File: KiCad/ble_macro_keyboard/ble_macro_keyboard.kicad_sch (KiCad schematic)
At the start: 29 parts, among them SW11 SW_Push, SW12 SW_Push, U1 MCP73831T-2ACI/OT, U2 ESP32-DEVKITC-32D

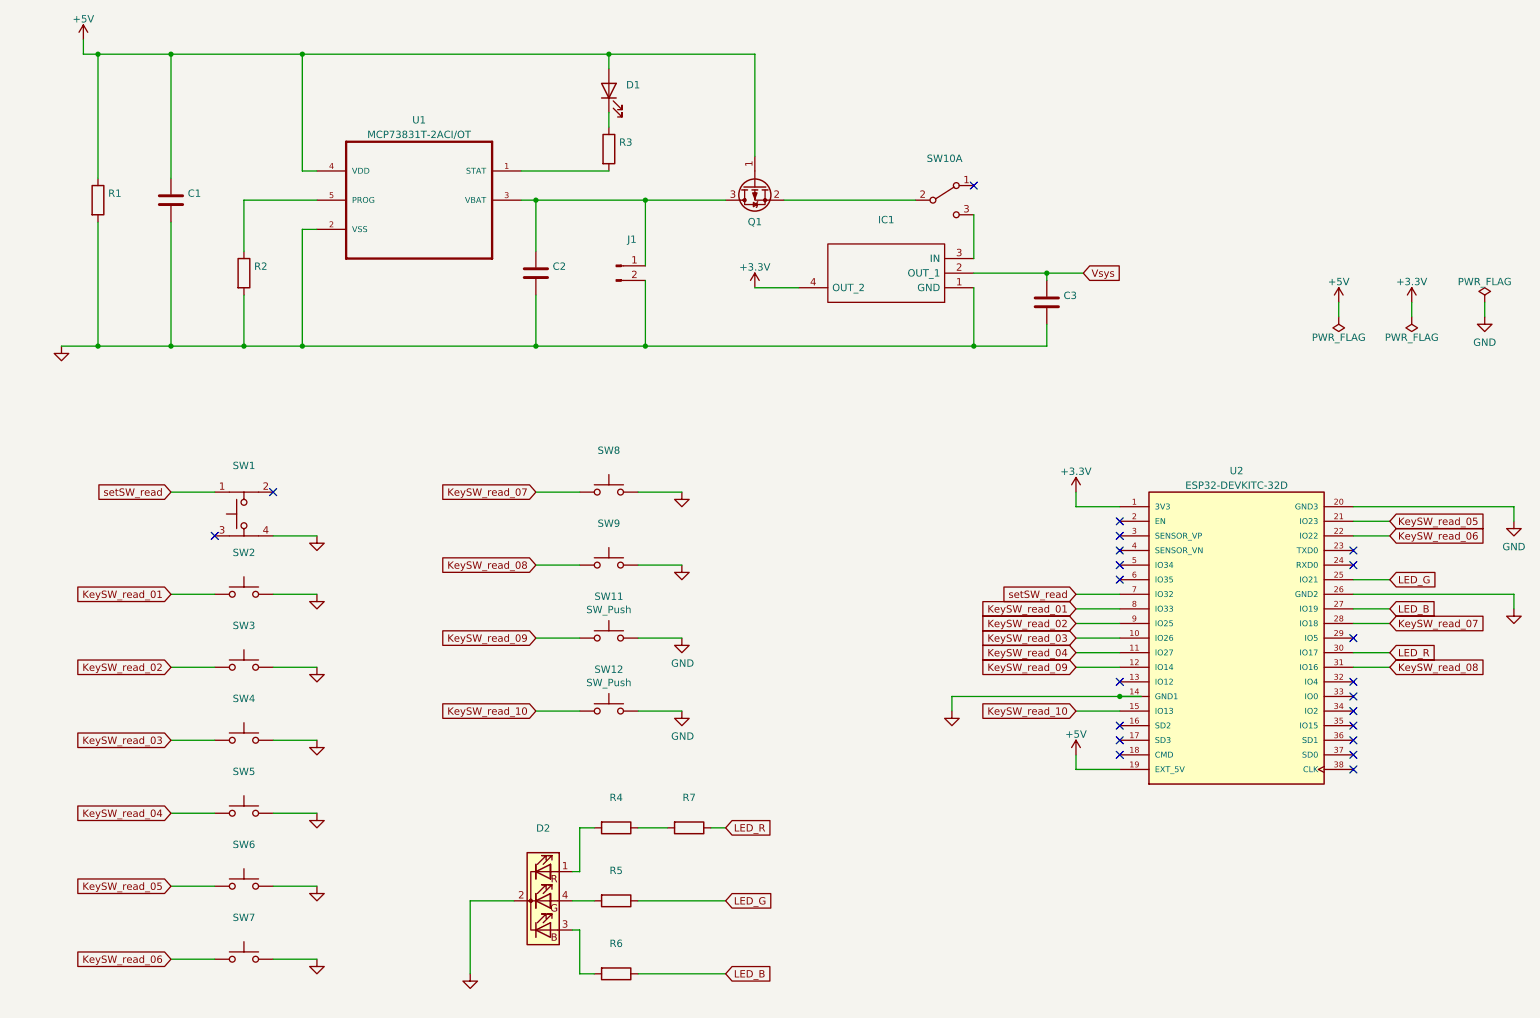
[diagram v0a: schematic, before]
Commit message: library replace and connect symbol to footprint.
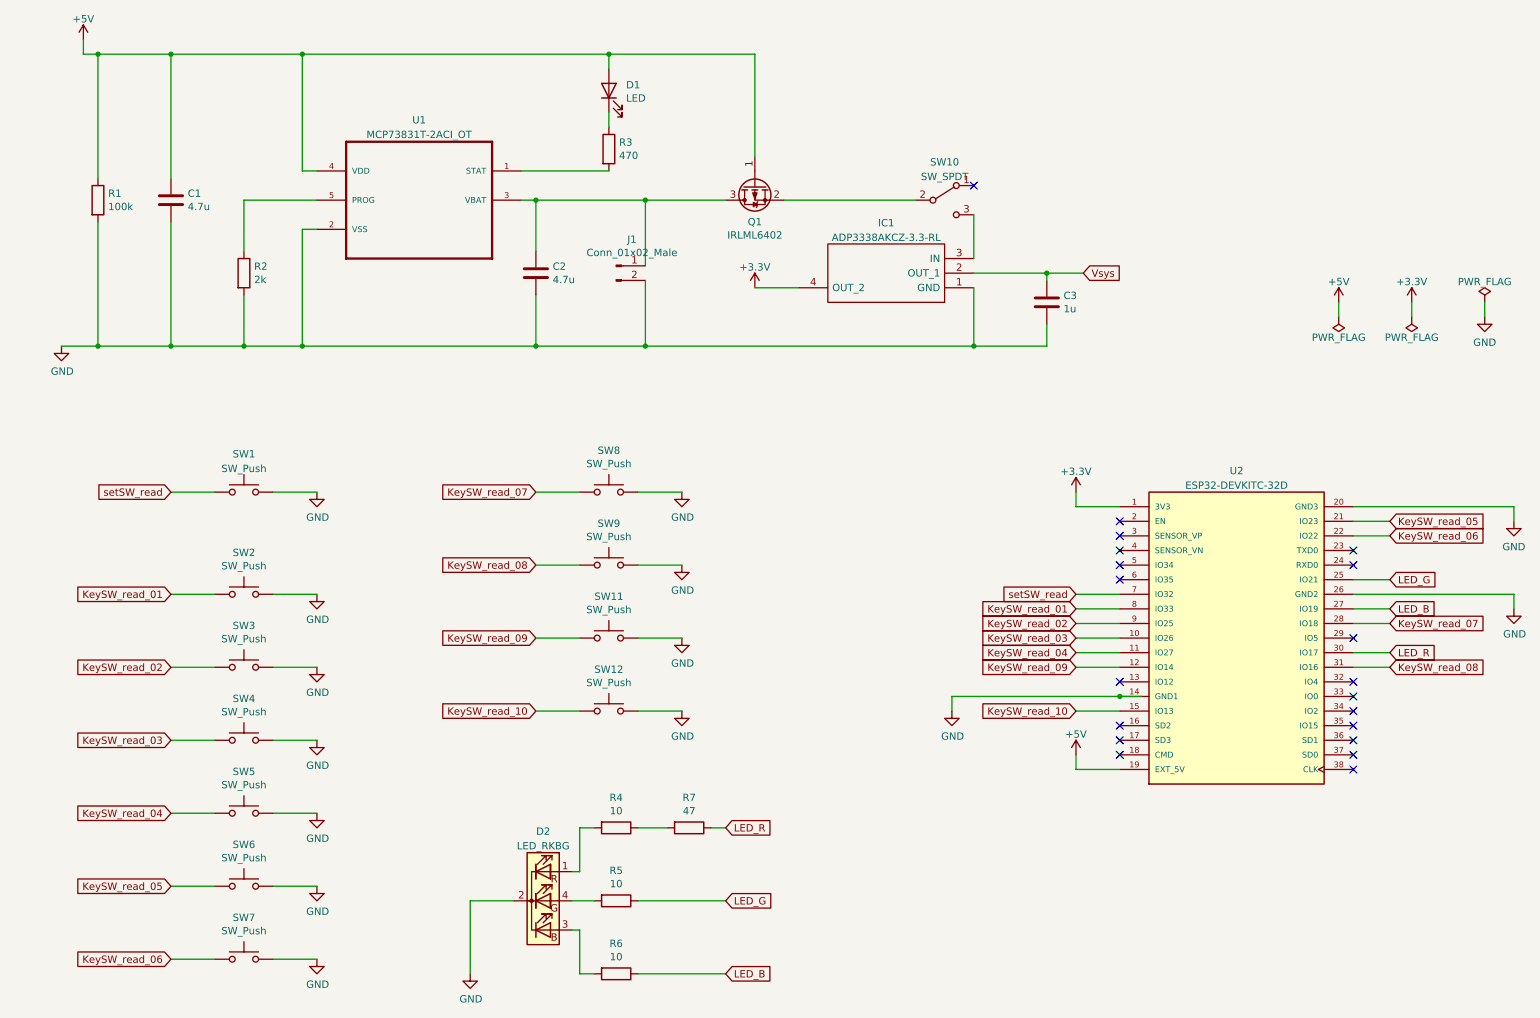
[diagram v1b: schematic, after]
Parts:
- removed D2: (no value), symbol ble_macro_keyboard-rescue:LED_RCBG-Device
- removed IC1: (no value), symbol Regulator_Linear_add:ADP3338AKCZ-3.3-RL
- removed SW1: (no value), symbol Switch_add:SW_SKRPACE010
- removed SW10: (no value), symbol Switch:SW_DPDT_x2
- removed U1: MCP73831T-2ACI/OT, SOT95P280X145-5N, symbol Battery_Management_add:MCP73831T-2ACI/OT
- added D2: LED_RKBG, LED_THT:LED_D5.0mm-4_RGB, symbol Device:LED_RKBG
- added IC1: ADP3338AKCZ-3.3-RL, Ble_keyboard:SOT230P700X180-4N, symbol ble_keyboard:ADP3338AKCZ-3.3-RL
- added SW1: SW_Push, Ble_keyboard:SW_Push_Dual_x2_TS-4401, symbol Switch:SW_Push
- added SW10: SW_SPDT, Ble_keyboard:SW_Slide_SPDT_MSK-12C02, symbol Switch:SW_SPDT
- added U1: MCP73831T-2ACI_OT, Ble_keyboard:SOT95P280X145-5N, symbol ble_keyboard:MCP73831T-2ACI_OT
- C1: value (none) -> 4.7u; footprint (none) -> Capacitor_THT:CP_Radial_D5.0mm_P2.00mm
- C2: value (none) -> 4.7u; footprint (none) -> Capacitor_SMD:C_0805_2012Metric_Pad1.15x1.40mm_HandSolder
- C3: value (none) -> 1u; footprint (none) -> Capacitor_SMD:C_0805_2012Metric_Pad1.15x1.40mm_HandSolder
- D1: value (none) -> LED; footprint (none) -> LED_THT:LED_D3.0mm
- J1: value (none) -> Conn_01x02_Male; footprint (none) -> Connector_JST:JST_SH_SM03B-SRSS-TB_1x03-1MP_P1.00mm_Horizontal
- Q1: value (none) -> IRLML6402; footprint (none) -> Package_TO_SOT_SMD:SOT-23
- R1: value (none) -> 100k; footprint (none) -> Resistor_SMD:R_0603_1608Metric_Pad1.05x0.95mm_HandSolder
- R2: value (none) -> 2k; footprint (none) -> Resistor_SMD:R_0603_1608Metric_Pad1.05x0.95mm_HandSolder
- R3: value (none) -> 470; footprint (none) -> Resistor_SMD:R_0603_1608Metric_Pad1.05x0.95mm_HandSolder
- R4, R5, R6: value (none) -> 10; footprint (none) -> Resistor_SMD:R_0603_1608Metric_Pad1.05x0.95mm_HandSolder
- R7: value (none) -> 47; footprint (none) -> Resistor_SMD:R_0603_1608Metric_Pad1.05x0.95mm_HandSolder
- SW2, SW3, SW4, SW5, SW6, SW7, SW8, SW9: value (none) -> SW_Push; footprint (none) -> Keyswitches:Kailh_socket_MX
- U2: footprint MODULE_ESP32-DEVKITC-32D -> Evaluation_board:MODULE_ESP32-DEVKITC-32D
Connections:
- net +3.3V: now also IC1.4 (OUT_2)
- net +5V: now also U1.4 (VDD)
- net GND: now also D2.2 (K), IC1.1 (GND), SW1.2, U1.2 (VSS)
- net Vsys: now also IC1.2 (OUT_1)
- net setSW_read: now also SW1.1
- net at R2.1: now also U1.5 (PROG)
- net at C2.1, J1.1 (Pin_1), Q1.3 (D): now also U1.3 (VBAT)
- net at Q1.2 (S): now also SW10.2 (B)
- net at R3.2: now also U1.1 (STAT)
- net at R5.2: now also D2.4 (GA)
- net at R4.2: now also D2.1 (RA)
- net at R6.2: now also D2.3 (BA)
- new net: IC1.3 (IN), SW10.3 (C)
- no-connect marks 22 -> 20

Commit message: keyswitch add to 12.
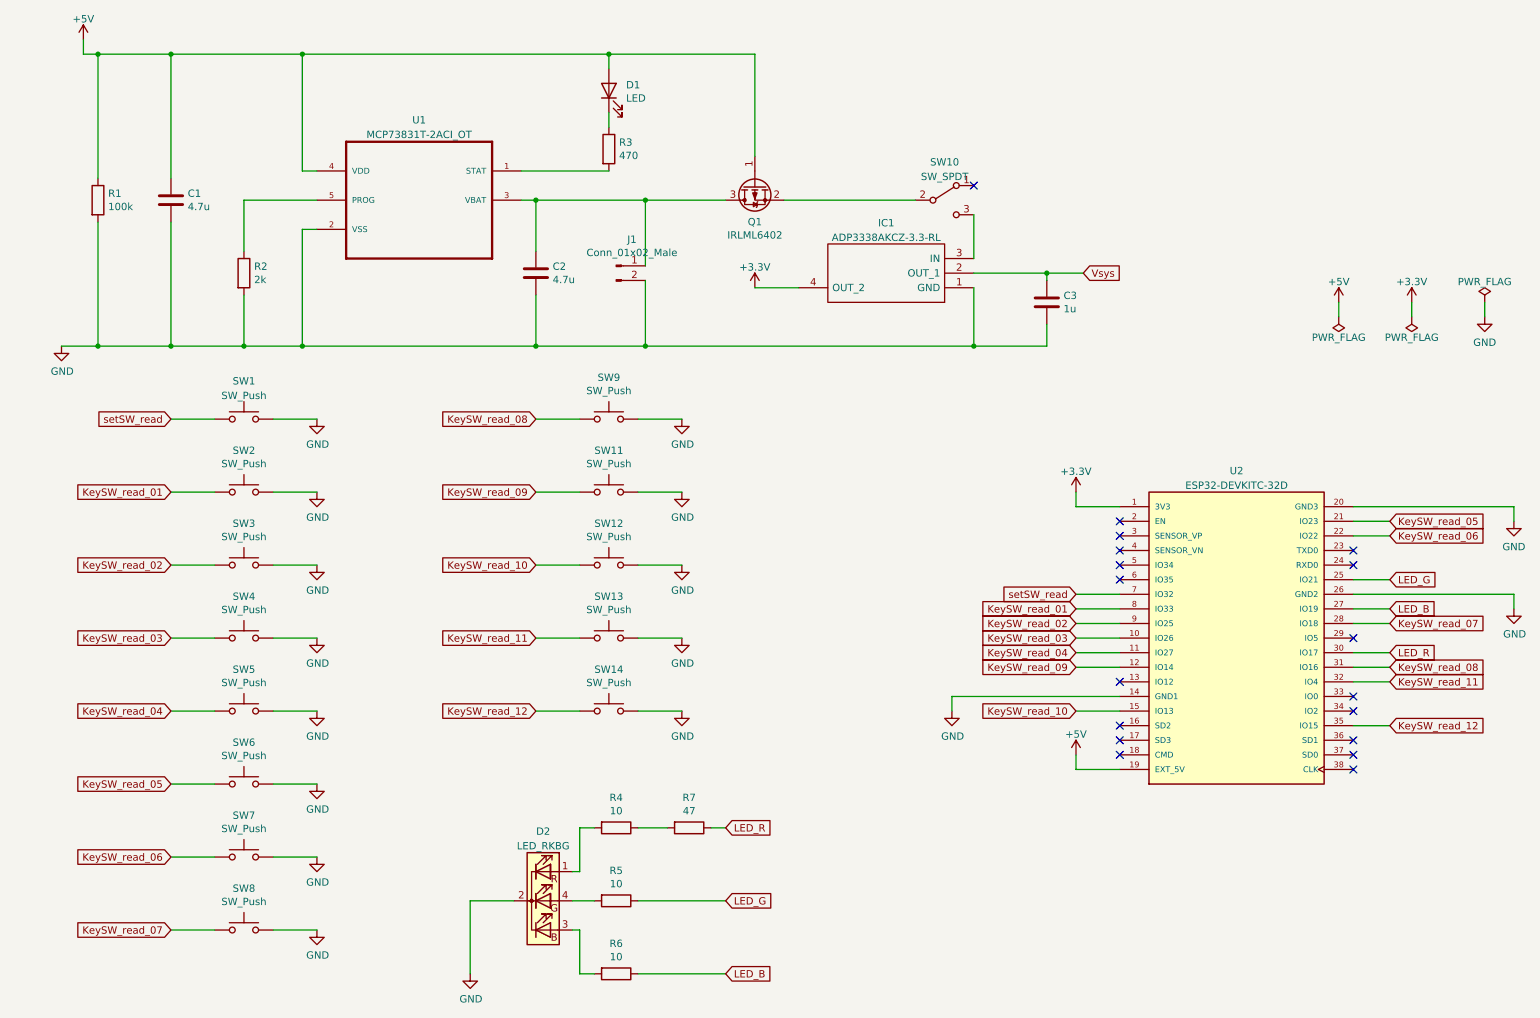
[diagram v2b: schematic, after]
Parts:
- added SW13, SW14: SW_Push, Keyswitches:Kailh_socket_MX, symbol Switch:SW_Push
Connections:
- net GND: now also SW13.2, SW14.2
- net KeySW_read_11: now reaches U2.32 (IO4)
- net KeySW_read_11: now also SW13.1
- net KeySW_read_12: now reaches U2.35 (IO15)
- net KeySW_read_12: now also SW14.1
- no-connect marks 20 -> 18
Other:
- moved on the sheet: SW1, SW11, SW12, SW2, SW3, SW4, SW5, SW6, SW7, SW8, SW9

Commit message: コネクタを除き、シンボルとフットプリントの紐づけ完了
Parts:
- removed J1: Conn_01x02_Male, Connector_JST:JST_SH_SM03B-SRSS-TB_1x03-1MP_P1.00mm_Horizontal, symbol Connector:Conn_01x02_Male
- added C1, C4: 0.01u, Capacitor_SMD:C_0603_1608Metric_Pad1.08x0.95mm_HandSolder, symbol Device:C
- added C5: 1u, Capacitor_SMD:C_0603_1608Metric_Pad1.08x0.95mm_HandSolder, symbol Device:C
- added J1: Conn_01x03_Male, symbol Connector:Conn_01x03_Male
- C3: renamed from C2; value 4.7u -> 10u; footprint Capacitor_SMD:C_0805_2012Metric_Pad1.15x1.40mm_HandSolder -> Capacitor_THT:CP_Radial_D5.0mm_P2.00mm
- C6: renamed from C3; footprint Capacitor_SMD:C_0805_2012Metric_Pad1.15x1.40mm_HandSolder -> Capacitor_SMD:C_0603_1608Metric_Pad1.08x0.95mm_HandSolder
- renumbered C1 to C2
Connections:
- net +5V: now also C1.1
- net GND: now also C1.2, C4.2, C5.2, J1.3 (Pin_3)
- net at C3.1, Q1.3 (D), U1.3 (VBAT): now also C4.1, J1.1 (Pin_1)
- net at Q1.2 (S), SW10.2 (B): now also C5.1
- net Battery_thermistor: now reaches U2.3 (SENSOR_VP)
- net Battery_thermistor: now also J1.2 (Pin_2)
- no-connect marks 18 -> 17
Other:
- moved on the sheet: C2, C3, C6, D1, IC1, Q1, R1, R2, R3, SW10, U1

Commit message: git submodule削除
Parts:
- J1: footprint (none) -> Ble_keyboard:JST_SHL_SM03B-SHLS-TF_1x03-1MP_P1.00mm_Horizontal
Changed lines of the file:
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@@
     (property "Reference" "J1" (id 0) (at 145.415 55.88 0))
     (property "Value" "Conn_01x03_Male" (id 1) (at 145.415 58.42 0))
-    (property "Footprint" "" (id 2) (at 144.78 63.5 0)
+    (property "Footprint" "Ble_keyboard:JST_SHL_SM03B-SHLS-TF_1x03-1MP_P1.00mm_Horizontal" (id 2) (at 144.78 63.5 0)
       (effects (font (size 1.27 1.27)) hide)
     )
@@
     )
     (path "/8a6a8ab4-f005-4e7a-89fa-0d032a129ddd"
-      (reference "J1") (unit 1) (value "Conn_01x03_Male") (footprint "")
+      (reference "J1") (unit 1) (value "Conn_01x03_Male") (footprint "Ble_keyboard:JST_SHL_SM03B-SHLS-TF_1x03-1MP_P1.00mm_Horizontal")
     )
     (path "/00000000-0000-0000-0000-000060aa8b9d"

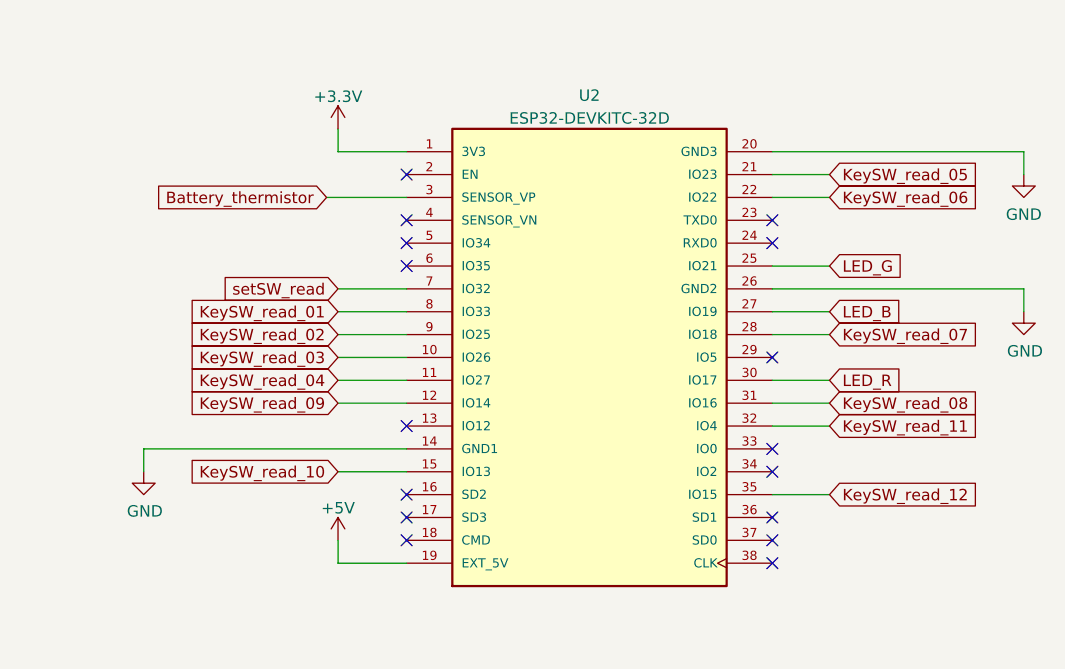
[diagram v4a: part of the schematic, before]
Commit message: 基板図配線のためにマイコンのピン入れ替え
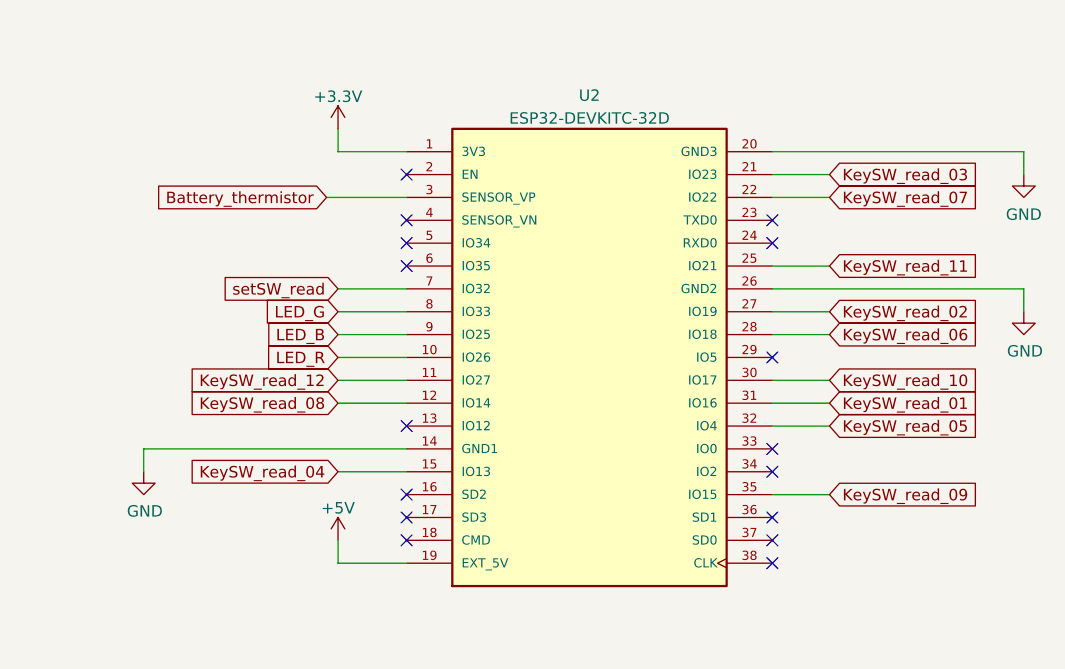
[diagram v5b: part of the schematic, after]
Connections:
- net KeySW_read_01: now also U2.31 (IO16); no longer U2.8 (IO33)
- net KeySW_read_02: now also U2.27 (IO19); no longer U2.9 (IO25)
- net KeySW_read_03: now also U2.21 (IO23); no longer U2.10 (IO26)
- net KeySW_read_04: now also U2.15 (IO13); no longer U2.11 (IO27)
- net KeySW_read_05: now also U2.32 (IO4); no longer U2.21 (IO23)
- net KeySW_read_06: now also U2.28 (IO18); no longer U2.22 (IO22)
- net KeySW_read_07: now also U2.22 (IO22); no longer U2.28 (IO18)
- net KeySW_read_08: now also U2.12 (IO14); no longer U2.31 (IO16)
- net KeySW_read_09: now also U2.35 (IO15); no longer U2.12 (IO14)
- net KeySW_read_10: now also U2.30 (IO17); no longer U2.15 (IO13)
- net KeySW_read_11: now also U2.25 (IO21); no longer U2.32 (IO4)
- net KeySW_read_12: now also U2.11 (IO27); no longer U2.35 (IO15)
- net LED_B: now also U2.9 (IO25); no longer U2.27 (IO19)
- net LED_G: now also U2.8 (IO33); no longer U2.25 (IO21)
- net LED_R: now also U2.10 (IO26); no longer U2.30 (IO17)

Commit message: リファレンス指定子を昇順に変更
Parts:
- renumbered C4 to C2, C5 to C3, C6 to C4, C2 to C5, C3 to C6, R5 to R1, R6 to R2, R4 to R3, R7 to R4, R3 to R5, R2 to R6, R1 to R7, SW10 to SW1, SW9 to SW10, SW1 to SW2, SW2 to SW3, SW3 to SW4, SW4 to SW5, SW5 to SW6, SW6 to SW7, SW7 to SW8, SW8 to SW9

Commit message: [fix] Vsysラベルを3.3vへ修正
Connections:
- net Vsys is gone; now on net +3.3V: C4.1, IC1.2 (OUT_1)
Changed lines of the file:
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@@
+    (stroke (width 0) (type default) (color 0 0 0 0))
+  )
+  (wire (pts (xy 247.65 60.96) (xy 247.65 63.5))
     (stroke (width 0) (type default) (color 0 0 0 0))
   )
@@
     (effects (font (size 1.27 1.27)) (justify right))
     (property "Intersheet References" "${INTERSHEET_REFS}" (id 0) (at 6.35 0 0)
-      (effects (font (size 1.27 1.27)) hide)
-    )
-  )
-  (global_label "Vsys" (shape input) (at 247.65 63.5 0) (fields_autoplaced)
-    (effects (font (size 1.27 1.27)) (justify left))
-    (property "Intersheet References" "${INTERSHEET_REFS}" (id 0) (at 50.8 0 0)
       (effects (font (size 1.27 1.27)) hide)
     )
@@
     (pin "1")
   )
+  (symbol (lib_id "power:+3.3V") (at 247.65 60.96 0) (unit 1)
+    (in_bom yes) (on_board yes) (fields_autoplaced)
+    (property "Reference" "#PWR06" (id 0) (at 247.65 64.77 0)
+      (effects (font (size 1.27 1.27)) hide)
+    )
+    (property "Value" "+3.3V" (id 1) (at 247.65 57.3842 0))
+    (property "Footprint" "" (id 2) (at 247.65 60.96 0)
+      (effects (font (size 1.27 1.27)) hide)
+    )
+    (property "Datasheet" "" (id 3) (at 247.65 60.96 0)
+      (effects (font (size 1.27 1.27)) hide)
+    )
+    (pin "1")
+  )
   (symbol (lib_id "Device:C") (at 182.88 63.5 0) (unit 1)
     (in_bom yes) (on_board yes)
@@
       (reference "#PWR05") (unit 1) (value "GND") (footprint "")
     )
+    (path "/9d608270-095f-4ff7-9a1b-725643051095"
+      (reference "#PWR06") (unit 1) (value "+3.3V") (footprint "")
+    )
     (path "/00000000-0000-0000-0000-000060abbc5a"

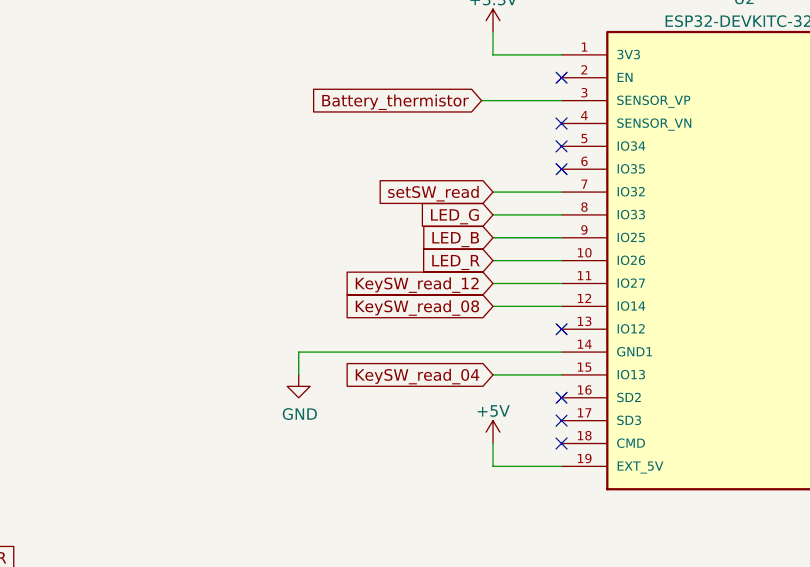
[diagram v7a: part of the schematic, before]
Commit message: [update] GND以外パターン接続
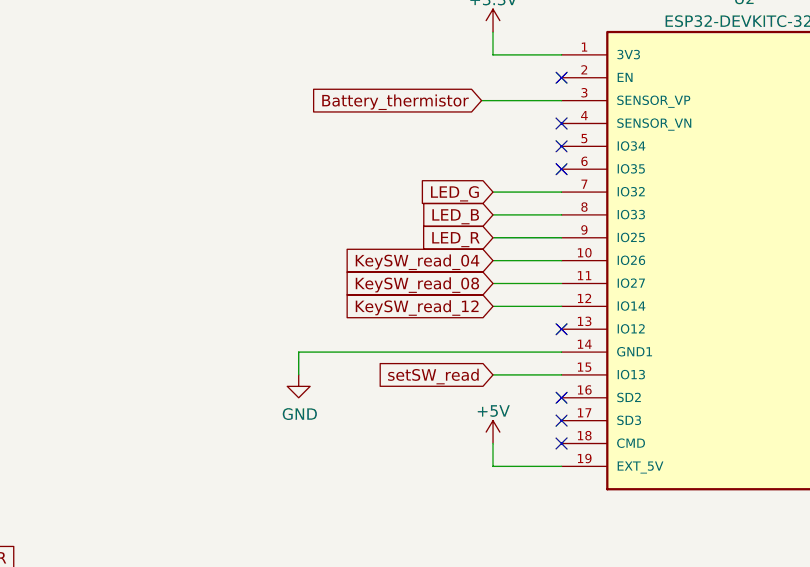
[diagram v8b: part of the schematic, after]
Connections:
- net KeySW_read_04: now also U2.10 (IO26); no longer U2.15 (IO13)
- net KeySW_read_08: now also U2.11 (IO27); no longer U2.12 (IO14)
- net KeySW_read_12: now also U2.12 (IO14); no longer U2.11 (IO27)
- net LED_B: now also U2.8 (IO33); no longer U2.9 (IO25)
- net LED_G: now also U2.7 (IO32); no longer U2.8 (IO33)
- net LED_R: now also U2.9 (IO25); no longer U2.10 (IO26)
- net setSW_read: now also U2.15 (IO13); no longer U2.7 (IO32)
